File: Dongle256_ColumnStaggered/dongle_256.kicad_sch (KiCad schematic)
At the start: 61 parts, among them SW1 GateronLP, SW10 GateronLP, SW11 GateronLP, SW12 GateronLP, SW13 GateronLP, SW14 GateronLP, SW15 GateronLP, SW16 GateronLP, SW17 GateronLP, SW18 GateronLP, SW19 GateronLP, SW2 GateronLP, SW20 GateronLP, SW21 GateronLP, SW22 GateronLP, SW23 GateronLP, SW24 GateronLP, SW25 GateronLP, SW26 GateronLP, SW27 GateronLP, SW28 GateronLP, SW29 GateronLP, SW3 GateronLP, SW30 GateronLP, SW4 GateronLP, SW5 GateronLP, SW6 GateronLP, SW7 GateronLP, SW8 GateronLP, SW9 GateronLP, U1 NRF52840-DONGLE

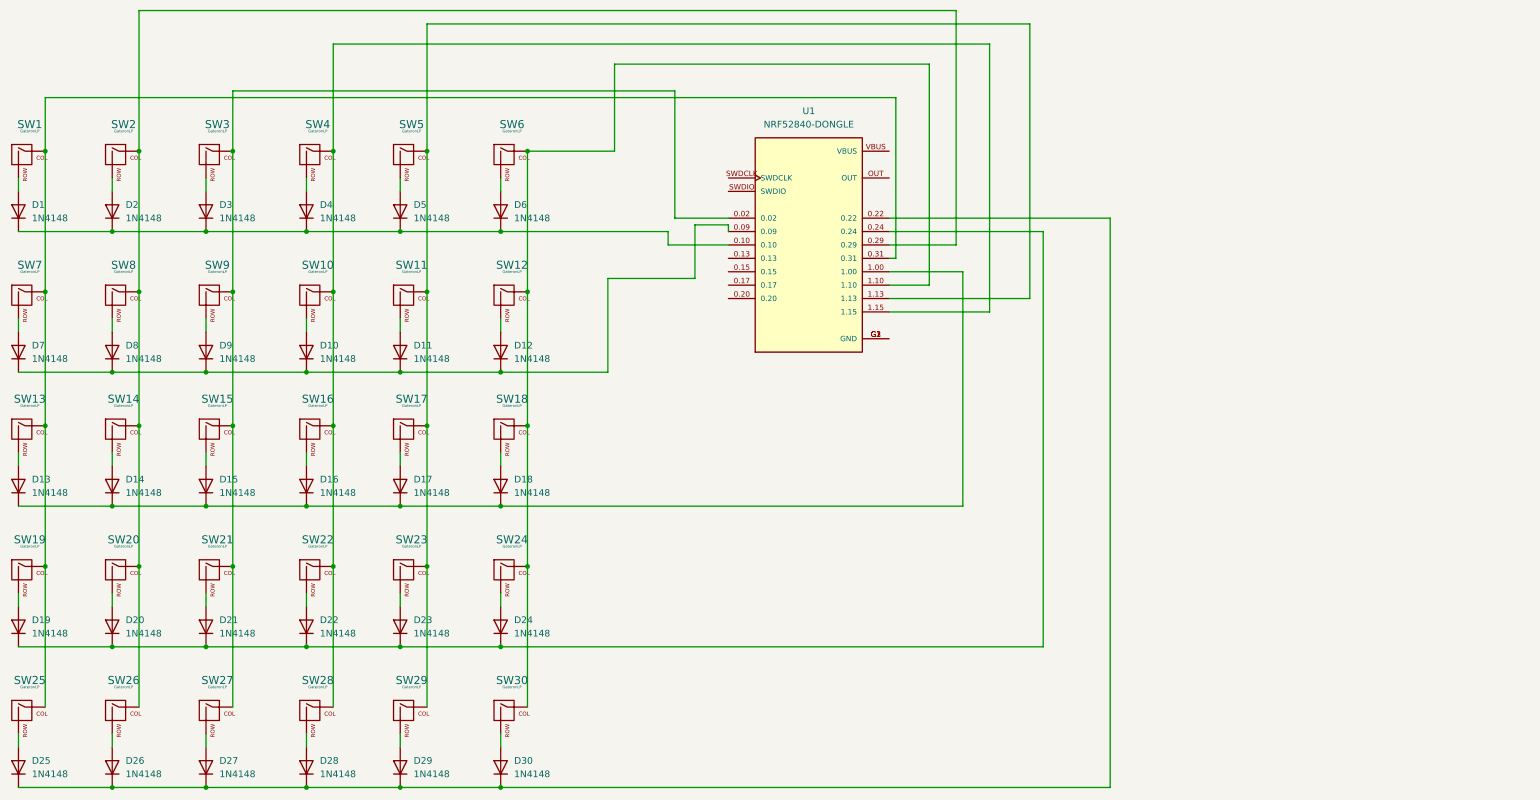
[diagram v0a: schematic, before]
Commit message: PCB design without switch
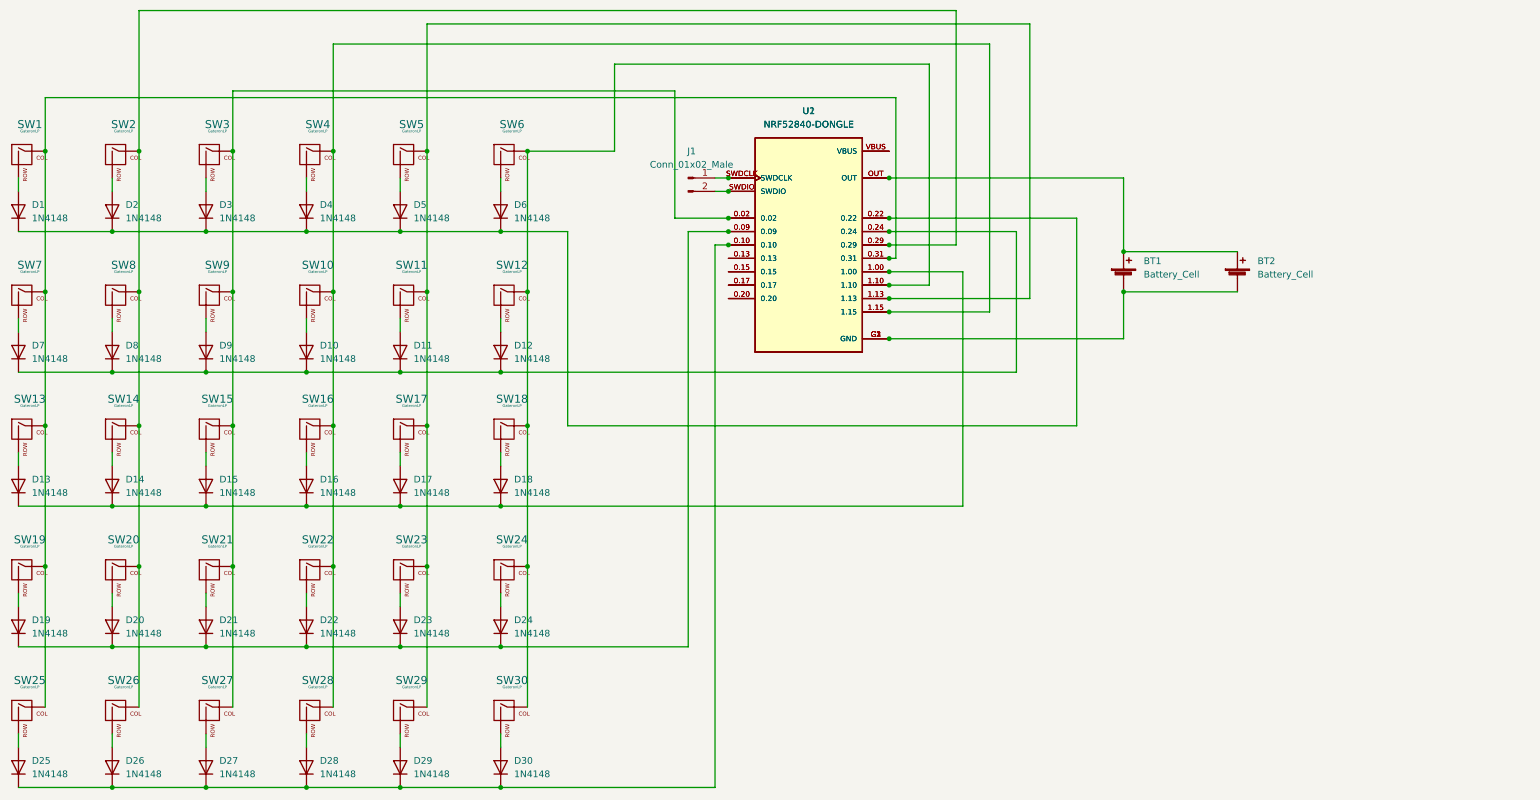
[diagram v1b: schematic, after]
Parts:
- added BT1, BT2: Battery_Cell, MVB:TBH-CR2032-M04, symbol Device:Battery_Cell
- added J1: Conn_01x02_Male, Connector_PinHeader_2.54mm:PinHeader_1x02_P2.54mm_Vertical, symbol Connector:Conn_01x02_Male
- added U2: NRF52840-DONGLE, download:MODULE_NRF52840-DONGLE, symbol NRF52840-DONGLE:NRF52840-DONGLE
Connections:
- net at D10.1 (K), D11.1 (K), D12.1 (K)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: now also U1.0.24, U2.0.24; no longer U1.0.09
- net at SW1.1 (COL), SW13.1 (COL), SW19.1 (COL)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: now also U2.0.31
- net at D25.1 (K), D26.1 (K), D27.1 (K)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: now also U1.0.10, U2.0.10; no longer U1.0.22
- net at SW12.1 (COL), SW18.1 (COL), SW24.1 (COL)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: now also U2.1.10
- net at D1.1 (K), D2.1 (K), D3.1 (K)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: now also U1.0.22, U2.0.22; no longer U1.0.10
- net at SW14.1 (COL), SW2.1 (COL), SW20.1 (COL)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: now also U2.0.29
- net at D13.1 (K), D14.1 (K), D15.1 (K)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: now also U2.1.00
- net at SW10.1 (COL), SW16.1 (COL), SW22.1 (COL)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: now also U2.1.15
- net at SW15.1 (COL), SW21.1 (COL), SW27.1 (COL)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: now also U2.0.02
- net at D19.1 (K), D20.1 (K), D21.1 (K)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: now also U1.0.09, U2.0.09; no longer U1.0.24
- net at SW11.1 (COL), SW17.1 (COL), SW23.1 (COL)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: now also U2.1.13
- net at U1.0.13: now also U2.0.13
- net at U1.0.15: now also U2.0.15
- net at U1.0.17: now also U2.0.17
- net at U1.0.20: now also U2.0.20
- net at U1.G1 (GND), U1.G2 (GND), U1.G3 (GND): now also BT1.2 (-), BT2.2 (-), U2.G1 (GND), U2.G2 (GND), U2.G3 (GND)
- net at U1.OUT: now also BT1.1 (+), BT2.1 (+), U2.OUT
- net at U1.SWDCLK: now also J1.1 (Pin_1), U2.SWDCLK
- net at U1.SWDIO: now also J1.2 (Pin_2), U2.SWDIO
- net at U1.VBUS: now also U2.VBUS

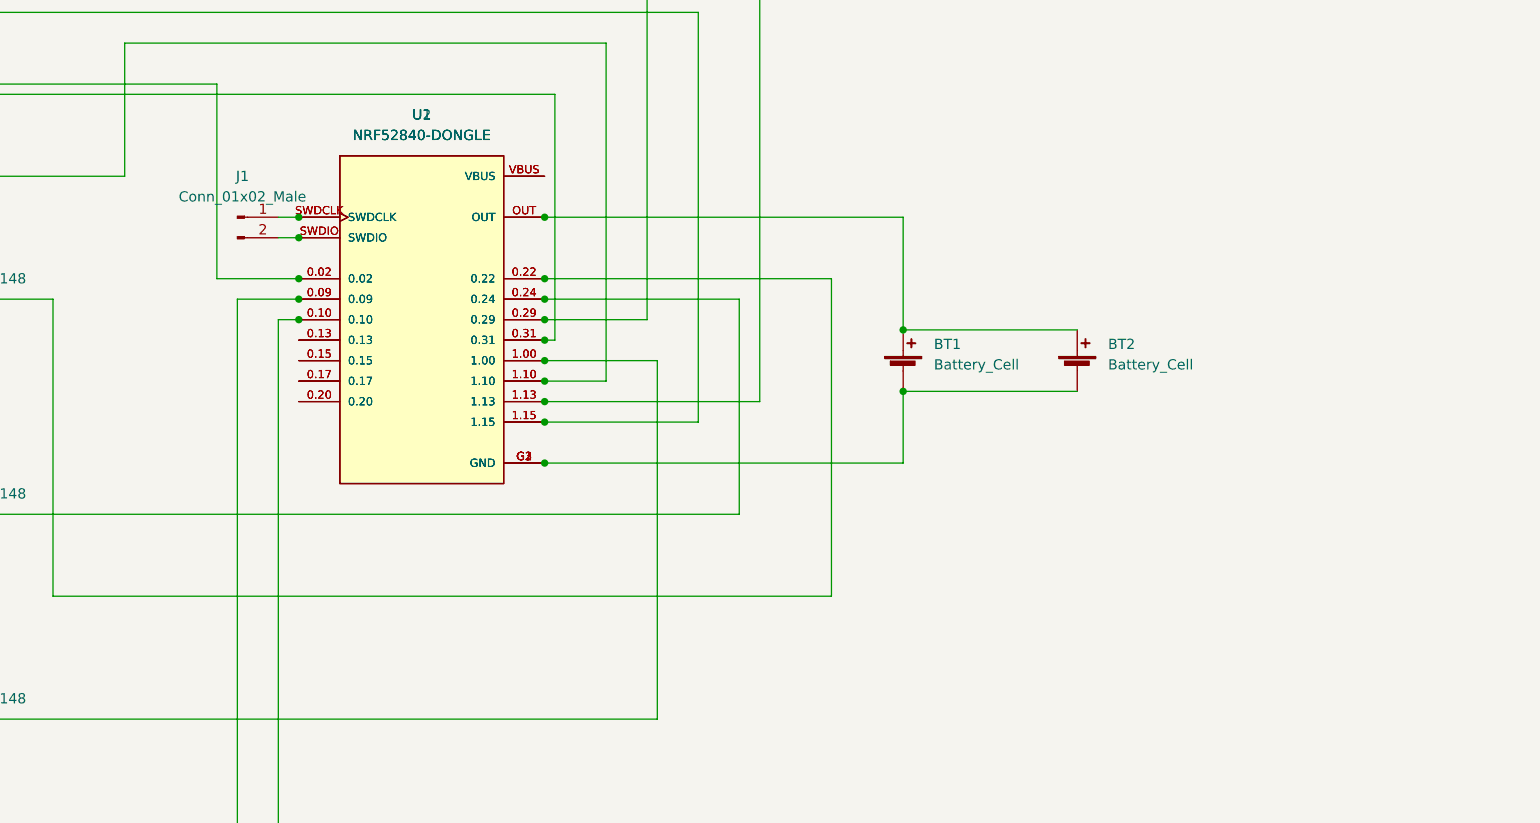
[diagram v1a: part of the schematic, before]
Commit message: Update on off and slider switch
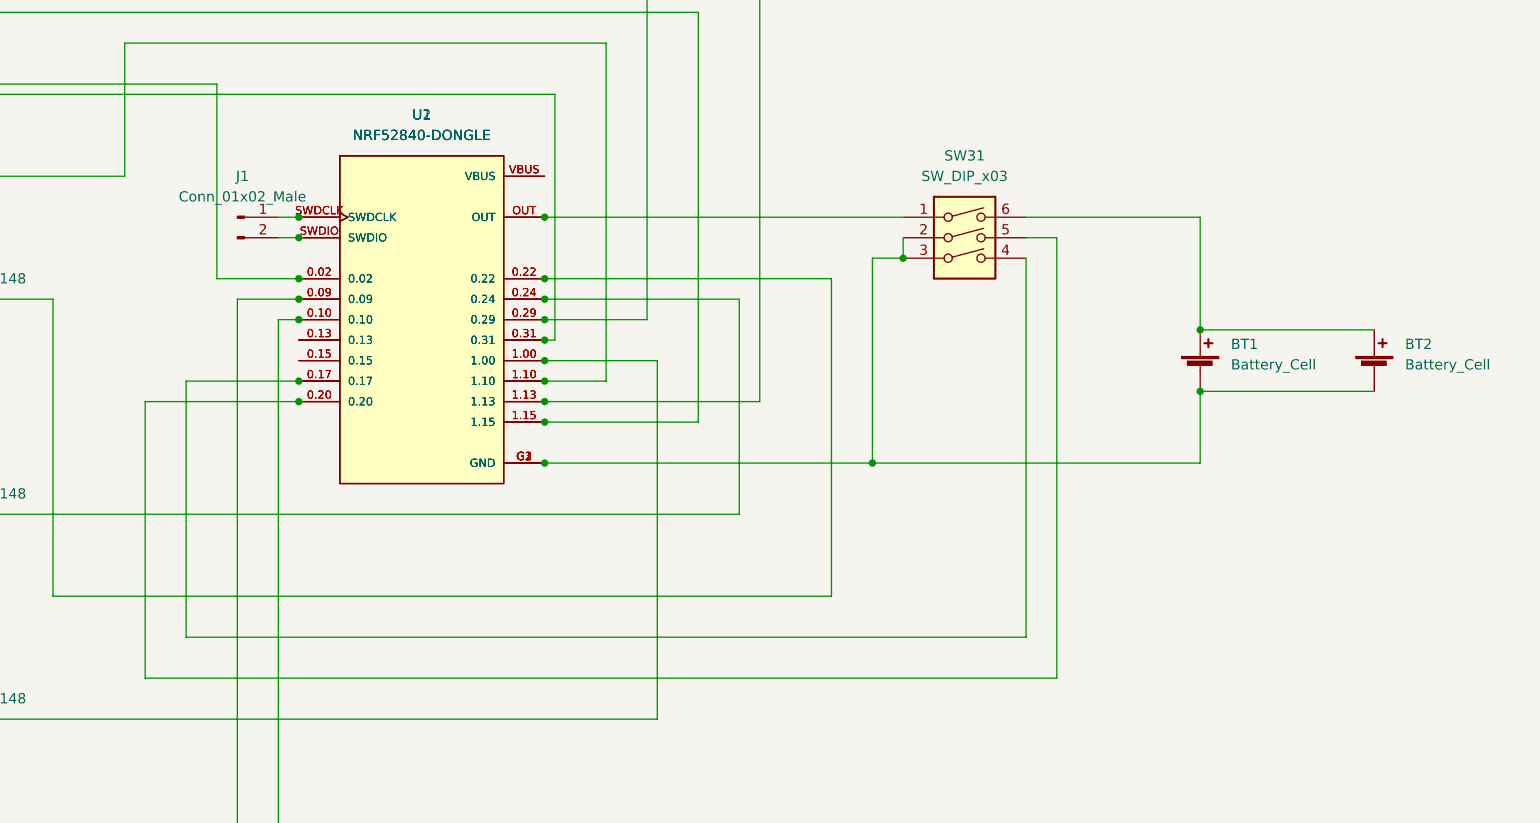
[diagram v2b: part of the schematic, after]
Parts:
- added SW31: SW_DIP_x03, Button_Switch_THT:SW_DIP_SPSTx03_Slide_9.78x9.8mm_W7.62mm_P2.54mm, symbol Switch:SW_DIP_x03
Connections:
- net at BT1.1 (+), BT2.1 (+): now also SW31.6; no longer U1.OUT, U2.OUT
- net at BT1.2 (-), BT2.2 (-), U1.G1 (GND)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: now also SW31.2, SW31.3
- net at U1.0.17, U2.0.17: now also SW31.4
- net at U1.0.20, U2.0.20: now also SW31.5
- new net: SW31.1, U1.OUT, U2.OUT
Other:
- moved on the sheet: BT1, BT2
